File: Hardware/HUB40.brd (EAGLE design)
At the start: 228.6 x 67.2 mm, 127 parts, among them U1 32U4, U2 USB_HUB_4_PORT, Y1 16MHz, Y2 12MHz

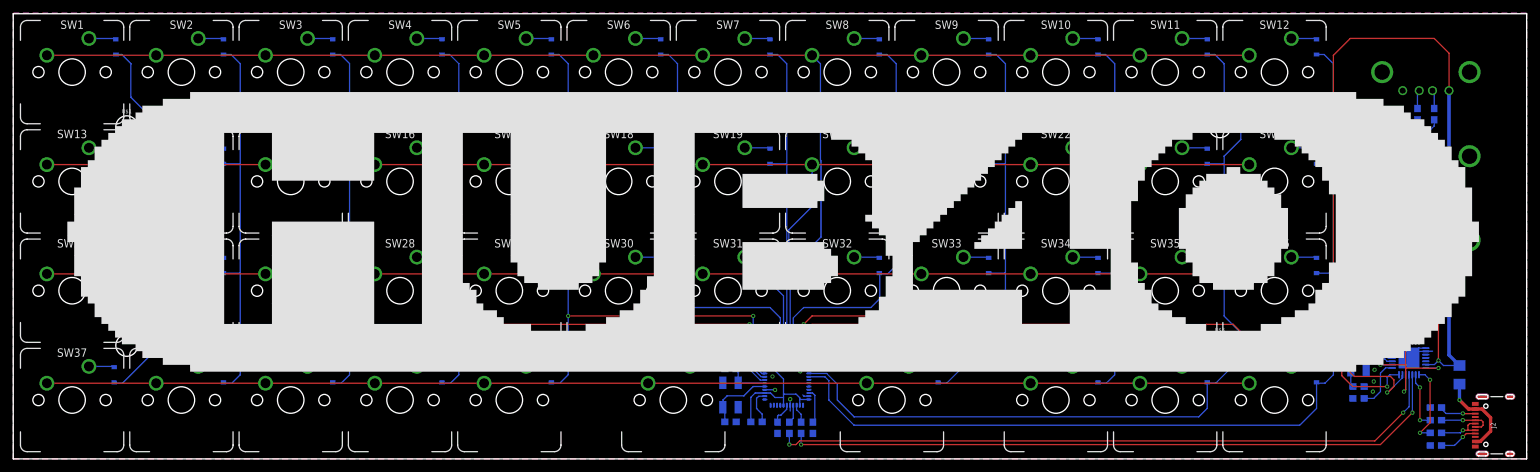
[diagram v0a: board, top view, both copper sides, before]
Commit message: Flipped Silkscreen
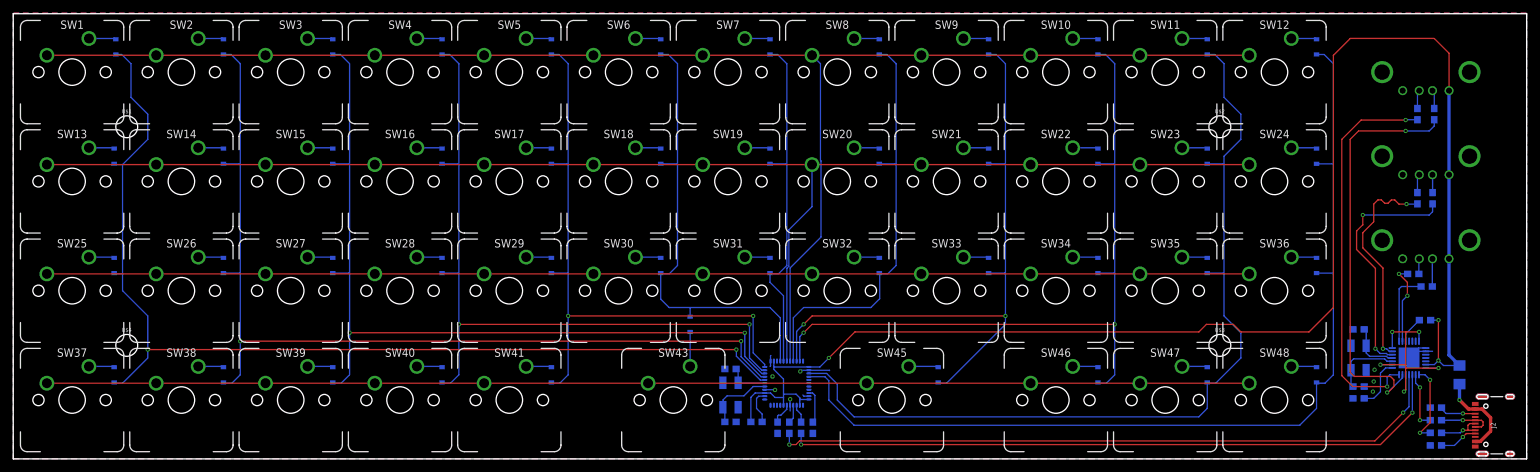
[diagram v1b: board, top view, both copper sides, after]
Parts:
- moved U$5 218.4 mm to (223.5, 33.0), flipped to the bottom
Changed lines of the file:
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@@
 <attribute name="VALUE" x="17.145" y="15.113" size="0.6096" layer="27" font="vector" ratio="20" align="top-center"/>
 </element>
-<element name="U$5" library="label" package="HUB400" value="" x="5.08" y="34.29" smashed="yes"/>
+<element name="U$5" library="label" package="HUB400" value="" x="223.52" y="33.02" smashed="yes" rot="MR0"/>
 </elements>
 <signals>
